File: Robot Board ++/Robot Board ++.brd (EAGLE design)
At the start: 76.2 x 76.2 mm, 24 parts, among them IC1 FT232RQ

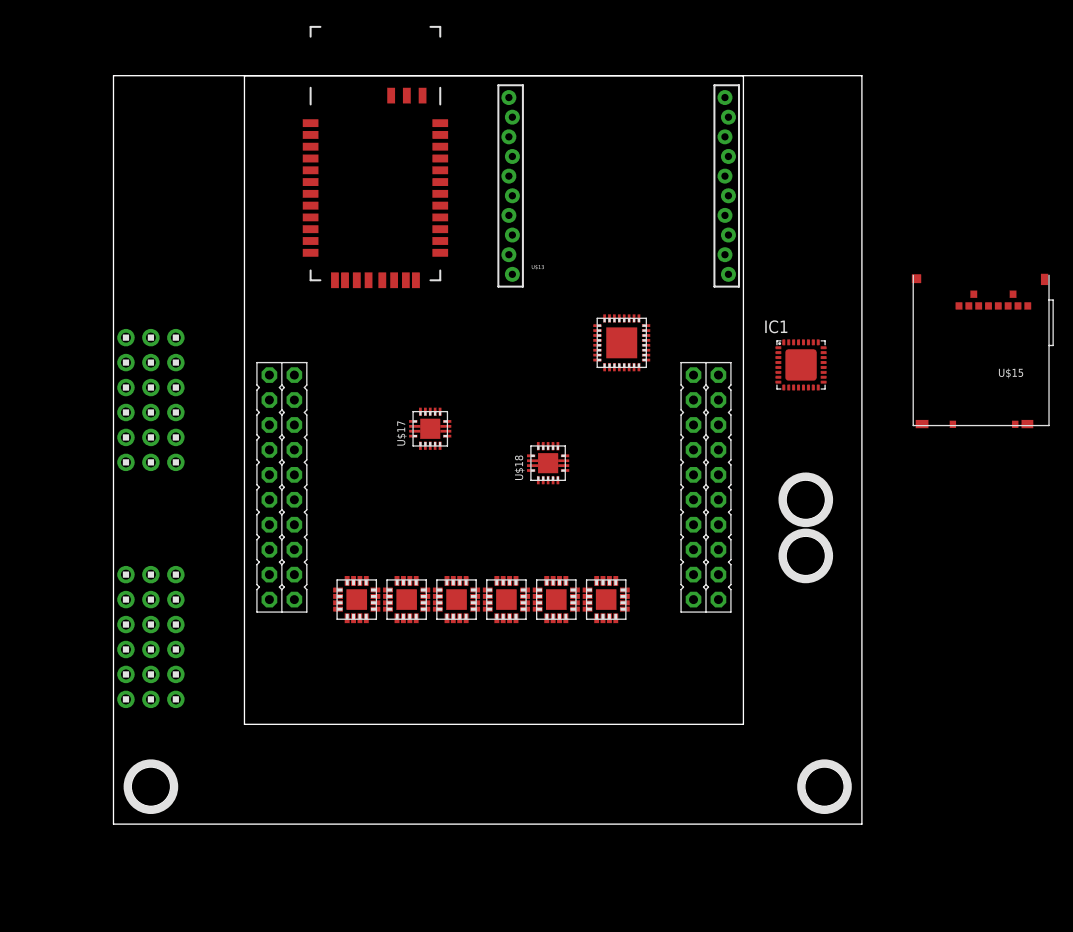
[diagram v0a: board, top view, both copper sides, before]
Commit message: Added headers for 4 Motors, 4 Quad Enc, 6 ADCs, 6 Servos, Analog Line Sensor, 4 Mosfets, 4 GPIO. Added 2 Dual Mosfet ICs, IMU IC Remved WiFi IC, FTDI IC
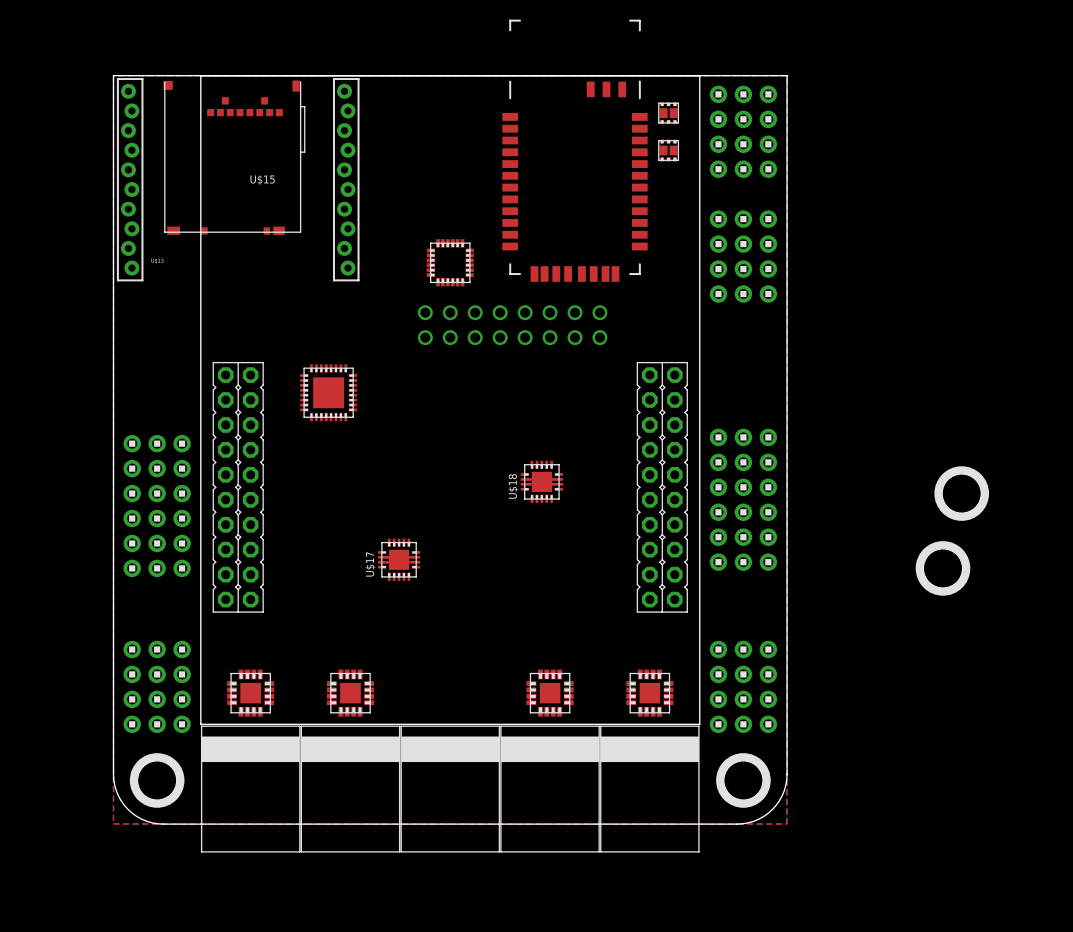
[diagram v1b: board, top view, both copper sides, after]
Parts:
- removed IC1: FT232RQ, ftdi:QFN32
- removed U$10: 1X6, headers(.1in):1X6
- removed U5, U6: (no value), packages(ti):RTY.16
- added U$1: 1X6, headers(.1in):1X6
- added U$29, U$30, U$32, U$33, U$60: 1X2.PTS, phoenixcontact:PTS.PLUG
- added U$35, U$36, U$37, U$38, U$39, U$40: 1X4, headers(.1in):1X4
- added U$43, U$44, U$45, U$46: 2X3, headers(.1in):2X3
- added U$55, U$56: FDMA1024NZ, freescale:MICROFET.2X2
- added U$59: MPU-6050, invensense:QFN.24.4X4
- added U$61: 2X8.TSW.D, headers(.1in)(samtec):TSW-108-XX-X-D-XXX
- moved U$15 78.7 mm to (19.1, 75.6)
- moved U$2 63.7 mm to (64.1, 26.7)
- moved U$5 58.7 mm to (61.6, 26.7)
- moved U$13 38.7 mm to (12.7, 54.6)
- moved U$16 30.3 mm to (21.9, 43.9)
- moved U$14 20.3 mm to (47.0, 65.4)
- moved U4 17.4 mm to (54.6, 13.3), turned to 0 degrees
- moved U$11 15.9 mm to (86.4, 33.7)
- moved U1 14.4 mm to (14.0, 13.3), turned to 0 degrees
- moved U$12 14.0 mm to (84.5, 26.0)
- moved U$17 13.7 mm to (29.1, 26.9)
- moved U3 13.5 mm to (44.5, 13.3), turned to 0 degrees
- moved U$6 11.7 mm to (1.91, 26.0)
- moved U2 11.1 mm to (24.1, 13.3), turned to 0 degrees
- moved U$4 8.28 mm to (64.1, 4.45)
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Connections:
- removed net VCC: IC1.19
- removed net VCCIO: IC1.1
- new net 5.0V: U$2.1, U$2.2, U$2.3, U$2.4, U$2.5, U$2.6
- new net AD0: U$9.1
- new net AD1: U$9.2
- new net AD2: U$9.3
- new net AD3: U$9.4
- new net AD4: U$9.5
- new net AD5: U$9.6
- new net E0.A: U$43.3
- new net E0.B: U$43.4
- new net E1.A: U$44.3
- new net E1.B: U$44.4
- new net E2.A: U$45.3
- new net E2.B: U$45.4
- new net E3.A: U$46.3
- new net E3.B: U$46.4
- new net FET0: U$37.1, U$55.2
- new net FET1: U$37.2, U$55.5
- new net FET2: U$37.3, U$56.2
- new net FET3: U$37.4, U$56.5
- new net IO0: U$40.1
- new net IO1: U$40.2
- new net IO2: U$40.3
- new net IO3: U$40.4
- new net M.!SLP: U1.3, U2.3, U3.3, U4.3
- new net M0+: U$29.2, U1.6
- new net M0-: U$29.1, U1.9
- new net M1+: U$30.2, U2.6
- new net M1-: U$30.1, U2.9
- new net M2+: U$32.2, U3.6
- new net M2-: U$32.1, U3.9
- new net M3+: U$33.2, U4.6
- new net M3-: U$33.1, U4.9
- new net N$1: U$38.4
- new net N$2: U$38.3
- new net N$3: U$38.2
- new net N$4: U$35.4
- new net N$5: U$35.3
- new net N$6: U$35.2
- new net SVRO0: U$5.1
- new net SVRO1: U$5.2
- new net SVRO2: U$5.3
- new net SVRO3: U$5.4
- new net SVRO4: U$5.5
- new net SVRO5: U$5.6
- net 3.3V: now also U$43.1, U$44.1, U$45.1, U$46.1, U$7.1, U$7.2, U$7.3, U$7.4, U$7.5, U$7.6
- net GND: now also U$1.1, U$1.2, U$1.3, U$1.4, U$1.5, U$1.6, U$43.2, U$44.2, U$45.2, U$46.2, U$55.1, U$55.4, U$56.1, U$56.4, U$6.1, U$6.2, U$6.3, U$6.4, U$6.5, U$6.6, U1.12, U1.2, U1.7, U1.PAD, U2.12, U2.2, U2.7, U2.PAD, U3.12, U3.2, U3.7, U3.PAD, U4.12, U4.2, U4.7, U4.PAD; no longer IC1.17, IC1.20, IC1.24, IC1.4
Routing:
- added copper zone on layer 1, net GND
- added copper zone on layer 16, net GND
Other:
- board size 76.2 x 76.2 mm -> 68.6 x 76.2 mm

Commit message: Finalized(?) board/headers layout Finalized LineSensor connector Connected ADC lines and Line Sensor to ADS7953
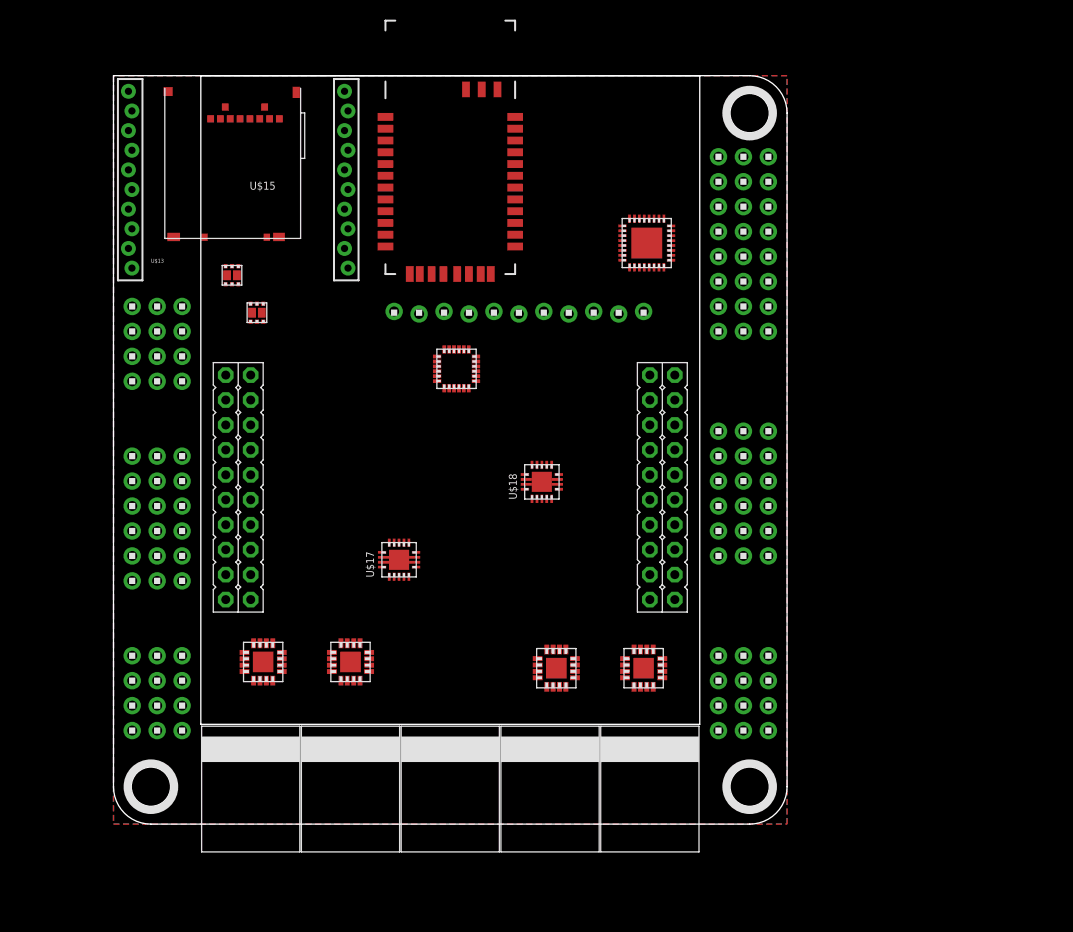
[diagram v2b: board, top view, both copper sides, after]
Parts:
- removed U$12: HOLE.4MM, screw_holes:4MM
- U$38, U$39, U$40: value 1X4 -> 1X6; device headers(.1in):1X4 -> headers(.1in):1X6
- U$6, U$7, U$9: value 1X6 -> 1X8; device headers(.1in):1X6 -> headers(.1in):1X8
- U$61: value 2X8.TSW.D -> 1X11.LOCK; device headers(.1in)(samtec):TSW-108-XX-X-D-XXX -> headers(.1in):1X11.LOCK
- moved U$6 77.1 mm to (66.7, 67.9), turned to 270 degrees
- moved U$7 72.9 mm to (64.1, 67.9), turned to 270 degrees
- moved U$9 68.8 mm to (61.6, 67.9), turned to 270 degrees
- moved U$35 68.3 mm to (1.91, 45.1)
- moved U$39 66.5 mm to (4.45, 24.8)
- moved U$38 66.5 mm to (1.91, 24.8)
- moved U$40 66.5 mm to (6.99, 24.8)
- moved U$36 63.5 mm to (4.45, 45.1)
- moved U$37 58.7 mm to (6.99, 45.1)
- moved U$56 47.4 mm to (12.1, 55.9)
- moved U$55 45.0 mm to (14.6, 52.1)
- moved U$11 44.3 mm to (64.8, 72.4)
- moved U$16 35.8 mm to (54.3, 59.2)
- moved U$61 13.4 mm to (54.0, 52.1), turned to 180 degrees
- moved U$14 12.7 mm to (34.3, 65.4)
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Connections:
- removed net N$6: U$35.2
- new net AD6: U$16.14, U$9.7
- new net AD7: U$16.13, U$9.8
- new net IO4: U$40.5
- new net IO5: U$40.6
- new net LS.1: U$16.5, U$61.8
- new net LS.2: U$16.6, U$61.7
- new net LS.3: U$16.7, U$61.6
- new net LS.4: U$16.8, U$61.5
- new net LS.5: U$16.9, U$61.4
- new net LS.6: U$16.10, U$61.3
- new net LS.7: U$16.11, U$61.2
- new net LS.8: U$16.12, U$61.1
- new net LS.LED: U$61.9
- new net LS.PWR: U$61.10
- new net N$19: U$14.13
- new net N$20: U$59.12
- new net N$21: U$14.14
- new net N$22: U$15.CD
- new net N$23: U$15.!CS!/NC/DAT3
- new net N$24: U$15.CLK
- new net N$25: U$15.MISO/DAT0
- new net N$26: U$15.MOSI/CMD
- net AD0: now also U$16.20
- net AD1: now also U$16.19
- net AD2: now also U$16.18
- net AD3: now also U$16.17
- net AD4: now also U$16.16
- net AD5: now also U$16.15
- net GND: now also U$14.1, U$14.12, U$14.25, U$14.27, U$14.28, U$14.29, U$15.GND, U$15.GND@1, U$15.GND@2, U$15.SHIELD, U$15.SHIELD@1, U$15.SHIELD@2, U$15.SHIELD@3, U$15.VSS, U$16.1, U$16.22, U$16.27, U$16.PAD, U$17.2, U$17.3, U$17.PAD, U$18.2, U$18.3, U$18.PAD, U$35.1, U$35.2, U$35.3, U$35.4, U$38.1, U$38.2, U$38.3, U$38.4, U$38.5, U$38.6, U$59.18, U$59.9, U$6.7, U$6.8, U$61.11
- net N$1: now also U$59.24; no longer U$38.4
- net N$2: now also U$59.23; no longer U$38.3
- net N$3: now also U$13.2; no longer U$38.2
- net N$4: now also U$13.3; no longer U$35.4
- net N$5: now also U$13.5; no longer U$35.3
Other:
- outline, holes or cut-outs redrawn

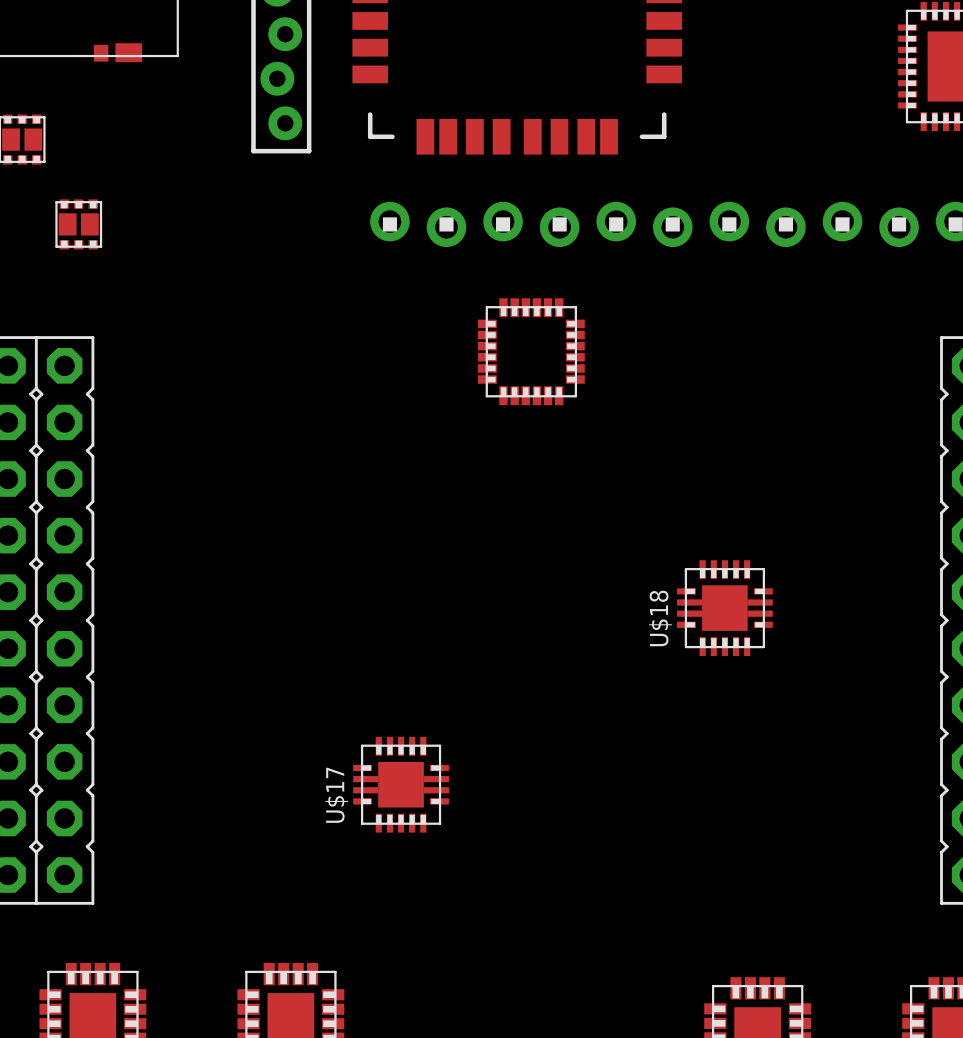
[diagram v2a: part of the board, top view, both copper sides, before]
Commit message: Completed schematic of Vbatt -> 5v regulator Began board layout of Vbatt -> 5v regulator
Considering bringing down max current supply from 8A to 6A (footprint for XAL1010 is large)

Switched to 11-pin header for Line Sensor
Created power select jumpters
Named serial signals
Added power supply signals
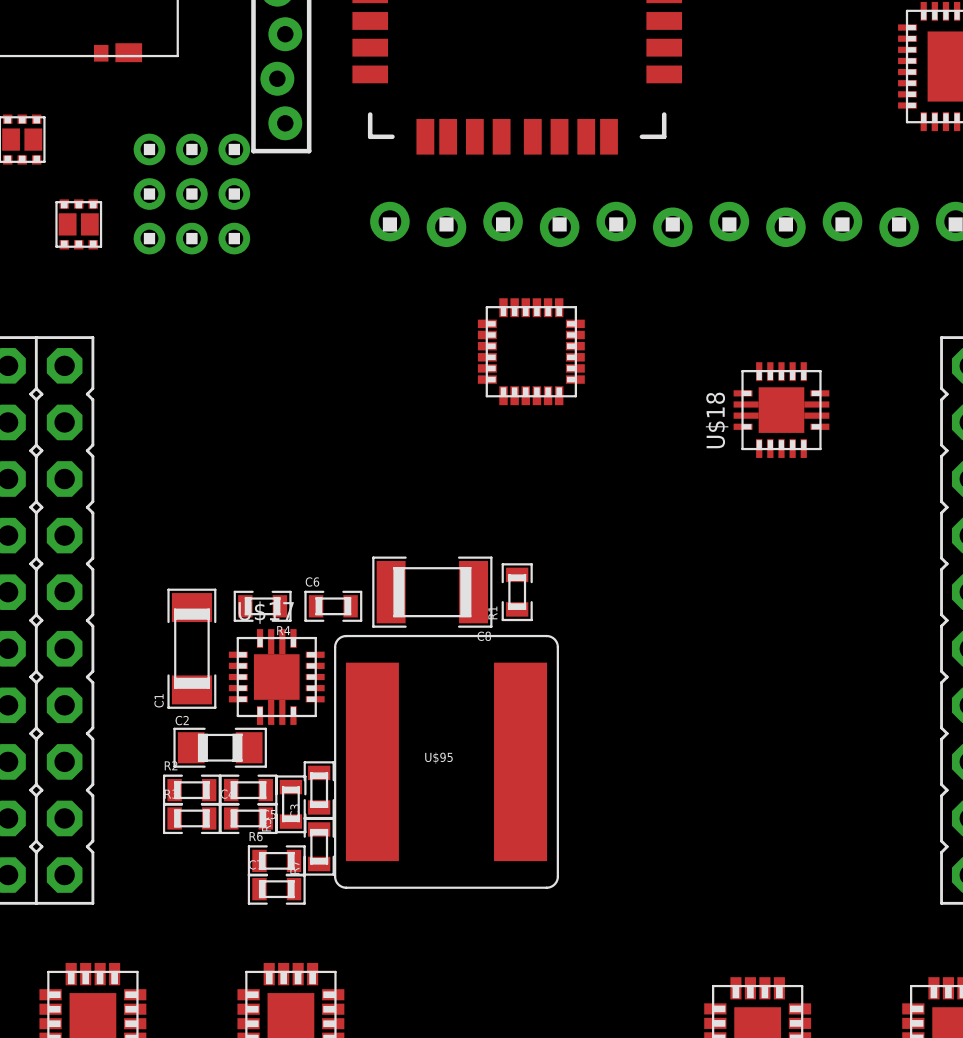
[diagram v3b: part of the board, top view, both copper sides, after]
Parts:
- added C1: 22uF, standardparts:1206
- added C2: 4.7uF, standardparts:0805
- added C3: 22nF, standardparts:0603
- added C4: 47nF, standardparts:0603
- added C5: 390pF, standardparts:0603
- added C6: .1uF, standardparts:0603
- added C7: 1nF, standardparts:0603
- added C8: 100uF, standardparts:1210
- added R1: 49.9k, standardparts:0603
- added R2: 31.2k, standardparts:0603
- added R3: 8.45, standardparts:0603
- added R4: 182k, standardparts:0603
- added R5: 1.81k, standardparts:0603
- added R6: 16.5k, standardparts:0603
- added R7: 2.21k, standardparts:0603
- added U$73, U$75, U$76: 1X3, headers(2mm):1X3
- added U$95: XAL1010-682, coilcraft:XAL1010
- moved U$18 9.25 mm to (46.2, 43.7)
- moved U$17 7.38 mm to (23.5, 31.8), turned to 270 degrees
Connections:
- net N$1 renamed IMU.SDA
- net N$19 renamed BT.TXO
- net N$2 renamed IMU.SCL
- net N$20 renamed IMU.INT
- net N$21 renamed BT.RXI
- net N$22 renamed SD.DETECT
- net N$23 renamed SD.!CS
- net N$24 renamed SD.SCLK
- net N$25 renamed SD.MISO
- net N$26 renamed SD.MOSI
- net N$3 renamed XBEE.RXI
- net N$4 renamed XBEE.TXO
- new net !RST: U$13.5, U$14.5
- new net ADS.!CS: U$16.23
- new net ADS.ALARM: U$16.29
- new net ADS.MISO: U$16.25
- new net ADS.MOSI: U$16.26
- new net ADS.SCLK: U$16.24
- new net BT.RESET: U$14.22
- new net N$1: R2.2, R3.1, U$17.10
- new net N$10: C6.2, U$17.11, U$17.12, U$95.P$1
- new net N$12: C7.2, R6.2, R7.1
- new net N$13: U$16.31
- new net N$2: R1.2, U$17.14
- new net N$3: C4.2, R5.1
- new net N$4: C5.1, R5.2, U$17.8
- new net N$6: U$16.2, U$16.3
- new net N$7: U$16.21, U$16.28, U$16.32
- new net N$8: R4.2, U$17.1
- new net N$9: C6.1, U$17.13
- new net VBAT: C1.1, C2.1, R1.1, R2.1, U$17.4, U$17.5, U$17.6, U$76.3
- new net VCC: U$7.1, U$7.2, U$7.3, U$7.4, U$7.5, U$7.6, U$7.7, U$7.8, U$75.2
- new net VDDIO: U$39.1, U$39.2, U$39.3, U$39.4, U$39.5, U$39.6, U$43.1, U$44.1, U$45.1, U$46.1, U$73.2
- new net VIN: U$36.1, U$36.2, U$36.3, U$36.4, U$76.2
- net 3.3V: now also U$73.1, U$75.1; no longer U$43.1, U$44.1, U$45.1, U$46.1, U$7.1, U$7.2, U$7.3, U$7.4, U$7.5, U$7.6
- net 5.0V: now also C7.1, C8.1, R6.1, U$17.7, U$73.3, U$75.3, U$76.1, U$95.P$2
- net GND: now also C1.2, C2.2, C3.1, C4.1, C5.2, C8.2, R3.2, R4.1, R7.2, U$16.30, U$16.4
- net N$5: now also C3.2, U$17.9; no longer U$13.5
